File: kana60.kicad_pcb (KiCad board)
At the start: 2 copper layers, 285.4 x 115.5 mm, 148 parts, among them SW1 SW_PUSH, SW10 SW_PUSH, SW11 SW_PUSH, SW12 SW_PUSH, SW13 SW_PUSH, SW14 SW_PUSH, SW15 SW_PUSH, SW16 SW_PUSH, SW17 SW_PUSH, SW18 SW_PUSH, SW19 SW_PUSH, SW2 SW_PUSH, SW20 SW_PUSH, SW21 SW_PUSH, SW22 SW_PUSH, SW23 SW_PUSH, SW24 SW_PUSH, SW25 SW_PUSH, SW26 SW_PUSH, SW27 SW_PUSH, SW28 SW_PUSH, SW29 SW_PUSH, SW3 SW_PUSH, SW30 SW_PUSH, SW31 SW_PUSH, SW32 SW_PUSH, SW33 SW_PUSH, SW34 SW_PUSH, SW35 SW_PUSH, SW36 SW_PUSH, SW37 SW_PUSH, SW38 SW_PUSH, SW39 SW_PUSH, SW4 SW_PUSH, SW40 SW_PUSH, SW41 SW_PUSH, SW42 SW_PUSH, SW43 SW_PUSH, SW44 SW_PUSH, SW45 SW_PUSH, SW46 SW_PUSH, SW47 SW_PUSH, SW48 SW_PUSH, SW49 SW_PUSH, SW5 SW_PUSH, SW50 SW_PUSH, SW51 SW_PUSH, SW52 SW_PUSH, SW53 SW_PUSH, SW54 SW_PUSH, SW55 SW_PUSH, SW56 SW_PUSH, SW57 SW_PUSH, SW58 SW_PUSH, SW59 SW_PUSH, SW6 SW_PUSH, SW60 SW_PUSH, SW61 SW_PUSH, SW62 SW_PUSH, SW63 SW_PUSH, SW64 SW_PUSH, SW65 SW_PUSH, SW66 SW_PUSH, SW67 SW_PUSH, SW68 SW_PUSH, SW69 SW_PUSH, SW7 SW_PUSH, SW70 SW_PUSH, SW71 SW_Push, SW8 SW_PUSH, SW9 SW_PUSH, U1 ProMicro

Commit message: trial and error
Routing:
- net col0: track 247.0 -> 647.6 mm
- net col1: track 235.3 -> 553.2 mm
- net col2: track 252.0 -> 501.0 mm
- net col3: track 229.0 -> 455.6 mm
- net col4: track 213.3 -> 369.7 mm
- net col5: track 235.9 -> 382.3 mm
- net col6: track 151.2 -> 192.0 mm
- net row1-0: track 91.7 -> 90.2 mm
- net row1-1: track 71.1 -> 70.0 mm
- net reset: track 44.6 -> 43.5 mm
- net Net-(D57-Pad2): track 180.4 -> 179.4 mm
- net Net-(D58-Pad2): track 140.7 -> 140.2 mm

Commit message: update
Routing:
- net col0: track 647.6 -> 501.7 mm
- net col1: track 553.2 -> 452.5 mm
- net col5: track 382.3 -> 291.1 mm, vias 0 -> 2
- net col3: track 455.6 -> 378.8 mm, vias 0 -> 2
- net col2: track 501.0 -> 444.4 mm
- net col4: track 369.7 -> 313.1 mm, vias 0 -> 2
- net col6: track 192.0 -> 228.8 mm
- net Net-(D57-Pad2): track 179.4 -> 144.0 mm
- net rs: track 168.7 -> 158.2 mm
- net Net-(D67-Pad2): track 292.9 -> 284.0 mm
- net Net-(D19-Pad2): track 134.6 -> 126.7 mm
- net Net-(D21-Pad2): track 100.0 -> 92.2 mm
- net Net-(D17-Pad2): track 168.4 -> 161.1 mm
- net Net-(D30-Pad2): track 98.7 -> 91.7 mm
- net Net-(D20-Pad2): track 135.5 -> 129.0 mm
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
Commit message: update
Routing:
- net Net-(D53-Pad2): track 182.9 -> 188.6 mm
- net Net-(D51-Pad2): track 143.7 -> 149.4 mm
- net Net-(D55-Pad2): track 229.3 -> 234.3 mm
- net Net-(D27-Pad2): track 84.5 -> 87.5 mm
- net Net-(D41-Pad2): track 185.9 -> 188.3 mm
- net Net-(D22-Pad2): track 94.4 -> 96.8 mm
- net Net-(D40-Pad2): track 193.6 -> 195.9 mm
- net Net-(D39-Pad2): track 147.3 -> 149.6 mm
- net Net-(D49-Pad2): track 108.6 -> 110.7 mm
- net Net-(D47-Pad2): track 97.3 -> 99.3 mm
- net col2: track 444.4 -> 446.3 mm
- net Net-(D43-Pad2): track 163.7 -> 165.6 mm
- net Net-(D24-Pad2): track 71.2 -> 72.8 mm
- net Net-(D42-Pad2): track 237.1 -> 238.3 mm
- net Net-(D20-Pad2): track 129.0 -> 130.2 mm
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
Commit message: connection complete
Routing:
- net row4-1: track 211.6 -> 206.1 mm
- net col2: track 446.3 -> 450.7 mm
- net col4: track 313.2 -> 316.6 mm
- net row2-1: track 192.8 -> 189.5 mm
- net row3-0: track 171.5 -> 169.0 mm
- net col3: track 378.8 -> 381.0 mm
- net row0-0: track 129.8 -> 128.0 mm
- net col0: track 501.7 -> 503.3 mm
- net col1: track 452.6 -> 454.1 mm
- net row2-0: track 150.0 -> 148.5 mm
- net col5: track 291.1 -> 292.5 mm
- net row1-0: track 90.5 -> 91.9 mm
- net row1-1: track 70.2 -> 71.4 mm
- net reset: track 44.1 -> 43.6 mm

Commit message: rotate reset switch
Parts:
- moved SW71 2.70 mm to (260.9, 21.8), turned to 180 degrees
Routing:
- net col4: track 316.6 -> 313.6 mm
- net reset: track 43.6 -> 46.1 mm
- net col3: track 381.0 -> 378.9 mm
- net col2: track 450.7 -> 448.8 mm
- net col1: track 454.1 -> 452.5 mm
- net col0: track 503.3 -> 502.0 mm
- net row1-1: track 71.4 -> 70.7 mm
- net row1-0: track 91.9 -> 91.2 mm
- net row3-1: track 228.8 -> 228.3 mm
- net row4-0: track 245.9 -> 245.3 mm

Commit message: update
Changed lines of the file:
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@@
     (thickness 1.6)
     (drawings 655)
-    (tracks 1100)
+    (tracks 1095)
     (zones 0)
     (modules 148)
@@
   (segment (start 105.653978 38.55771) (end 163.30722 38.55771) (width 0.25) (layer B.Cu) (net 9))
   (segment (start 25.71 25.7677) (end 42.49015 25.7677) (width 0.25) (layer B.Cu) (net 10))
-  (segment (start 42.49015 25.7677) (end 44.39515 23.8627) (width 0.25) (layer F.Cu) (net 10))
-  (segment (start 250.862288 26.416) (end 255.915688 26.416) (width 0.25) (layer F.Cu) (net 10))
+  (segment (start 262.900688 26.416) (end 265.453988 23.8627) (width 0.25) (layer F.Cu) (net 10))
   (segment (start 248.308988 23.8627) (end 250.862288 26.416) (width 0.25) (layer F.Cu) (net 10))
-  (segment (start 255.915688 26.416) (end 258.468988 23.8627) (width 0.25) (layer F.Cu) (net 10))
   (segment (start 265.453988 23.8627) (end 267.358988 21.9577) (width 0.25) (layer F.Cu) (net 10))
-  (segment (start 258.468988 23.8627) (end 265.453988 23.8627) (width 0.25) (layer F.Cu) (net 10))
+  (segment (start 42.49015 25.7677) (end 44.39515 23.8627) (width 0.25) (layer F.Cu) (net 10))
   (segment (start 44.39515 23.8627) (end 248.308988 23.8627) (width 0.25) (layer F.Cu) (net 10))
+  (segment (start 250.862288 26.416) (end 262.900688 26.416) (width 0.25) (layer F.Cu) (net 10))
   (segment (start 186.79944 39.00656) (end 186.79944 33.3877) (width 0.25) (layer B.Cu) (net 11))
   (segment (start 186.182 39.624) (end 186.79944 39.00656) (width 0.25) (layer B.Cu) (net 11))
@@
   (segment (start 170.01929 33.3877) (end 170.01929 41.593002) (width 0.25) (layer F.Cu) (net 17))
   (segment (start 45.84618 25.7677) (end 62.62633 25.7677) (width 0.25) (layer B.Cu) (net 18))
-  (segment (start 257.058688 27.178) (end 259.103988 25.1327) (width 0.25) (layer F.Cu) (net 18))
-  (segment (start 269.263988 25.1327) (end 269.898988 24.4977) (width 0.25) (layer F.Cu) (net 18))
-  (segment (start 64.03663 27.178) (end 257.058688 27.178) (width 0.25) (layer F.Cu) (net 18))
   (segment (start 269.898988 24.4977) (end 269.898988 21.9577) (width 0.25) (layer F.Cu) (net 18))
-  (segment (start 259.103988 25.1327) (end 269.263988 25.1327) (width 0.25) (layer F.Cu) (net 18))
+  (segment (start 267.218688 27.178) (end 269.898988 24.4977) (width 0.25) (layer F.Cu) (net 18))
+  (segment (start 64.03663 27.178) (end 267.218688 27.178) (width 0.25) (layer F.Cu) (net 18))
   (segment (start 62.62633 25.7677) (end 64.03663 27.178) (width 0.25) (layer F.Cu) (net 18))
   (segment (start 193.5115 45.950188) (end 193.468988 45.9927) (width 0.25) (layer F.Cu) (net 19))
@@
   (segment (start 47.752 45.230712) (end 47.752 54.755712) (width 0.25) (layer F.Cu) (net 75))
   (segment (start 46.993988 44.4727) (end 47.752 45.230712) (width 0.25) (layer F.Cu) (net 75))
+  (segment (start 47.498 28.448) (end 47.498 43.968688) (width 0.25) (layer F.Cu) (net 75))
   (segment (start 47.498 43.968688) (end 46.993988 44.4727) (width 0.25) (layer F.Cu) (net 75))
-  (segment (start 47.498 28.956) (end 47.498 43.968688) (width 0.25) (layer F.Cu) (net 75))
   (segment (start 282.598988 21.9577) (end 282.598988 27.535012) (width 0.25) (layer F.Cu) (net 75))
-  (segment (start 282.194 27.94) (end 48.514 27.94) (width 0.25) (layer F.Cu) (net 75))
-  (segment (start 48.514 27.94) (end 47.498 28.956) (width 0.25) (layer F.Cu) (net 75))
+  (segment (start 48.006 27.94) (end 47.498 28.448) (width 0.25) (layer F.Cu) (net 75))
+  (segment (start 282.194 27.94) (end 48.006 27.94) (width 0.25) (layer F.Cu) (net 75))
   (segment (start 282.598988 27.535012) (end 282.194 27.94) (width 0.25) (layer F.Cu) (net 75))
   (segment (start 80.021488 120.6727) (end 77.950238 120.6727) (width 0.25) (layer F.Cu) (net 76))
@@
   (segment (start 100.076 92.792212) (end 100.076 83.267212) (width 0.25) (layer F.Cu) (net 76))
   (segment (start 108.906488 101.6227) (end 100.076 92.792212) (width 0.25) (layer F.Cu) (net 76))
-  (segment (start 86.36 29.083) (end 86.741 28.702) (width 0.25) (layer F.Cu) (net 76))
-  (segment (start 84.455 29.591) (end 84.963 29.083) (width 0.25) (layer F.Cu) (net 76))
-  (segment (start 84.455 43.833712) (end 84.455 29.591) (width 0.25) (layer F.Cu) (net 76))
   (segment (start 285.138988 28.297012) (end 285.138988 21.9577) (width 0.25) (layer F.Cu) (net 76))
   (segment (start 284.734 28.702) (end 285.138988 28.297012) (width 0.25) (layer F.Cu) (net 76))
-  (segment (start 86.741 28.702) (end 284.734 28.702) (width 0.25) (layer F.Cu) (net 76))
-  (segment (start 84.963 29.083) (end 86.36 29.083) (width 0.25) (layer F.Cu) (net 76))
+  (segment (start 84.455 29.21) (end 84.963 28.702) (width 0.25) (layer F.Cu) (net 76))
   (segment (start 85.093988 44.4727) (end 84.455 43.833712) (width 0.25) (layer F.Cu) (net 76))
+  (segment (start 84.455 43.833712) (end 84.455 29.21) (width 0.25) (layer F.Cu) (net 76))
+  (segment (start 84.963 28.702) (end 284.734 28.702) (width 0.25) (layer F.Cu) (net 76))
   (segment (start 114.323988 78.4652) (end 118.431488 82.5727) (width 0.25) (layer F.Cu) (net 77))
   (segment (start 114.323988 64.1777) (end 114.323988 78.4652) (width 0.25) (layer F.Cu) (net 77))
@@
   (segment (start 119.126 98.806) (end 120.142 99.822) (width 0.25) (layer F.Cu) (net 77))
   (segment (start 118.431488 82.5727) (end 119.126 83.267212) (width 0.25) (layer F.Cu) (net 77))
-  (segment (start 125.476 39.624) (end 123.193988 41.906012) (width 0.25) (layer F.Cu) (net 77))
   (segment (start 123.193988 41.906012) (end 123.193988 44.4727) (width 0.25) (layer F.Cu) (net 77))
+  (segment (start 125.476 39.624) (end 123.193988 41.906012) (width 0.25) (layer F.Cu) (net 77))
   (segment (start 128.778 39.624) (end 125.476 39.624) (width 0.25) (layer F.Cu) (net 77))
+  (segment (start 131.445 30.099) (end 131.445 36.957) (width 0.25) (layer F.Cu) (net 77))
+  (segment (start 132.08 29.464) (end 131.445 30.099) (width 0.25) (layer F.Cu) (net 77))
   (segment (start 292.758988 29.059012) (end 292.354 29.464) (width 0.25) (layer F.Cu) (net 77))
-  (segment (start 132.334 29.464) (end 131.445 30.353) (width 0.25) (layer F.Cu) (net 77))
-  (segment (start 292.354 29.464) (end 132.334 29.464) (width 0.25) (layer F.Cu) (net 77))
   (segment (start 131.445 36.957) (end 128.778 39.624) (width 0.25) (layer F.Cu) (net 77))
-  (segment (start 131.445 30.353) (end 131.445 36.957) (width 0.25) (layer F.Cu) (net 77))
+  (segment (start 292.354 29.464) (end 132.08 29.464) (width 0.25) (layer F.Cu) (net 77))
   (segment (start 292.758988 21.9577) (end 292.758988 29.059012) (width 0.25) (layer F.Cu) (net 77))
   (segment (start 290.218988 25.042988) (end 290.218988 37.1977) (width 0.25) (layer B.Cu) (net 78))
@@
   (via (at 280.058988 30.988) (size 0.8) (drill 0.4) (layers F.Cu B.Cu) (net 80))
   (segment (start 279.296988 30.226) (end 280.058988 30.988) (width 0.25) (layer F.Cu) (net 80))
-  (segment (start 162.306 30.226) (end 279.296988 30.226) (width 0.25) (layer F.Cu) (net 80))
-  (segment (start 161.293988 31.238012) (end 162.306 30.226) (width 0.25) (layer F.Cu) (net 80))
-  (segment (start 161.293988 44.4727) (end 161.293988 31.238012) (width 0.25) (layer F.Cu) (net 80))
+  (segment (start 162.052 30.226) (end 279.296988 30.226) (width 0.25) (layer F.Cu) (net 80))
+  (segment (start 161.293988 30.984012) (end 162.052 30.226) (width 0.25) (layer F.Cu) (net 80))
+  (segment (start 161.293988 44.4727) (end 161.293988 30.984012) (width 0.25) (layer F.Cu) (net 80))
   (segment (start 257.198988 128.1297) (end 257.198988 121.3277) (width 0.25) (layer B.Cu) (net 81))
   (segment (start 238.021988 128.0027) (end 238.529988 128.5107) (width 0.25) (layer B.Cu) (net 81))

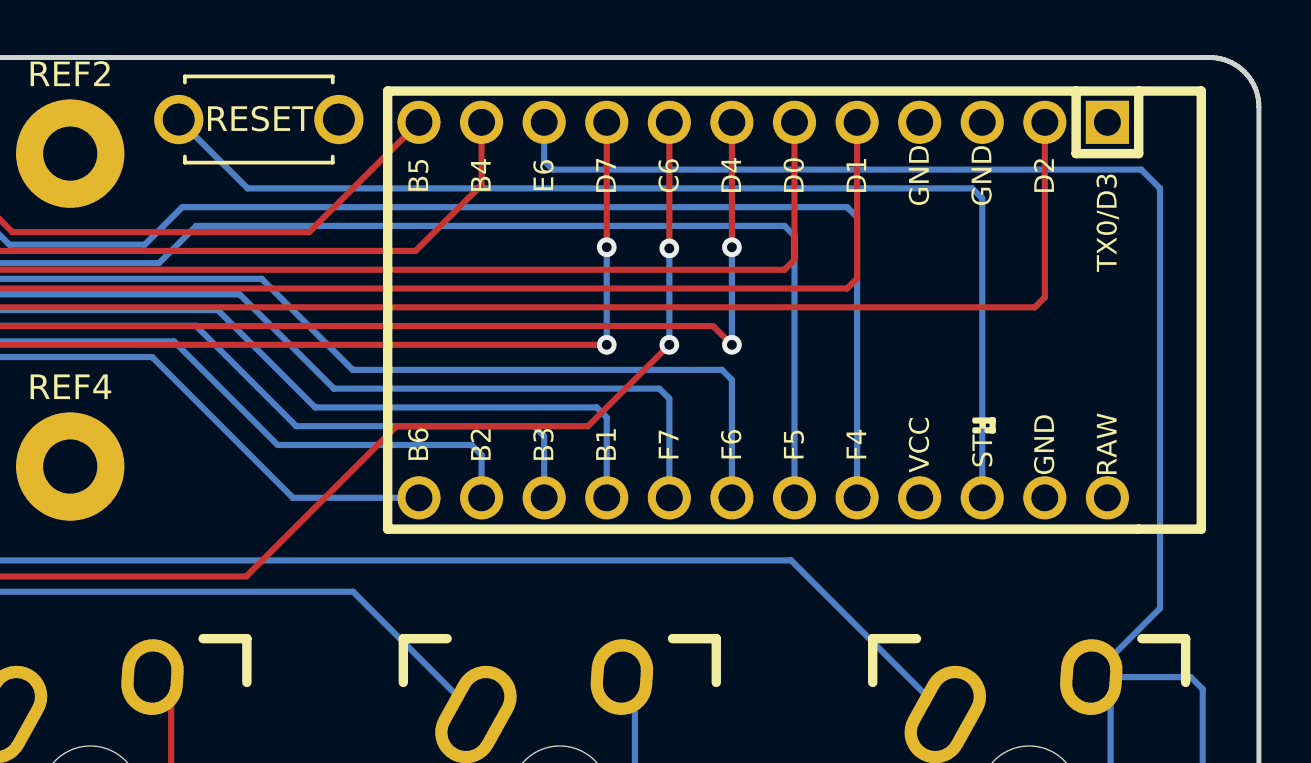
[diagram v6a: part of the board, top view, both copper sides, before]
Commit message: add text
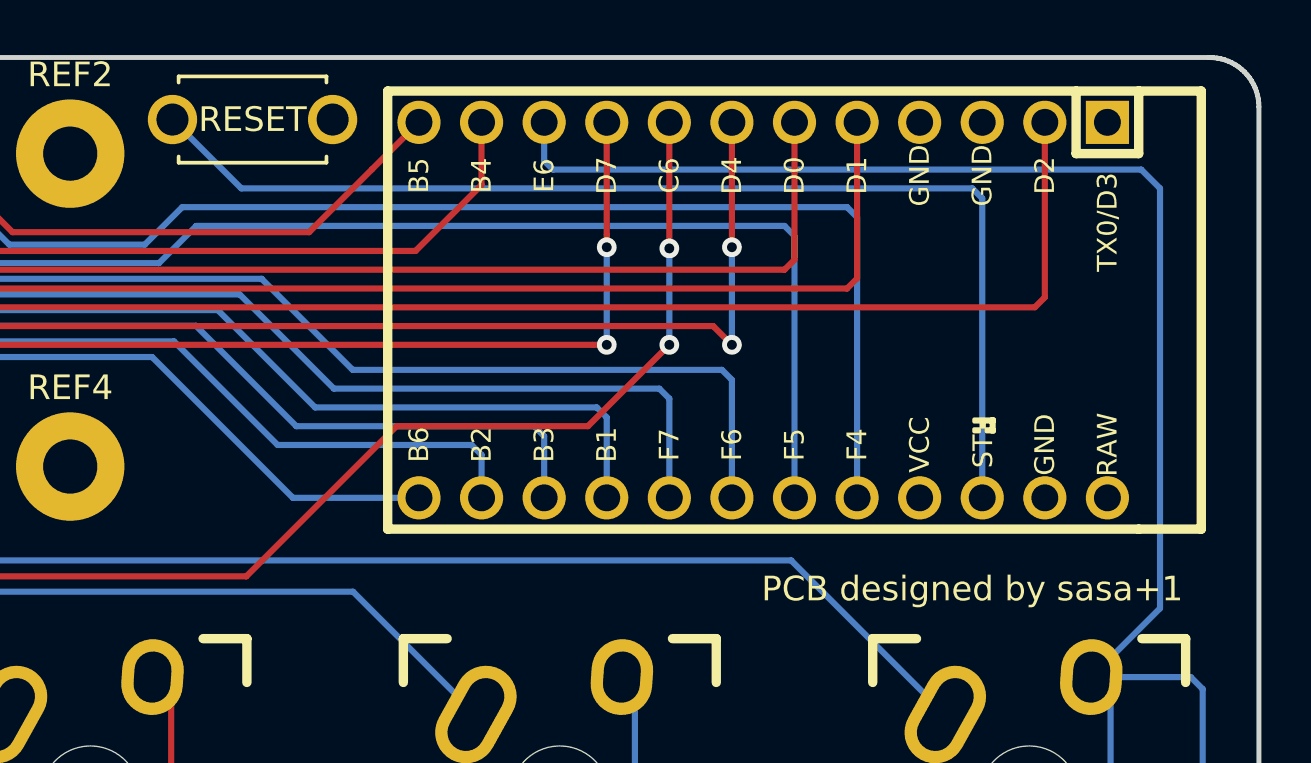
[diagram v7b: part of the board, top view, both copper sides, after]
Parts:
- moved SW71 0.25 mm to (260.6, 21.8)
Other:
- board text added: "PCB designed by sasa+1"
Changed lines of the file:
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@@
   (general
     (thickness 1.6)
-    (drawings 655)
+    (drawings 656)
     (tracks 1095)
     (zones 0)
@@
       (padsonsilk false)
       (subtractmaskfromsilk false)
-      (outputformat 1)
+      (outputformat 4)
       (mirror false)
-      (drillshape 1)
+      (drillshape 0)
       (scaleselection 1)
       (outputdirectory ""))
@@
   )
   (module kbd:ResetSW (layer F.Cu)
-    (at 260.858 21.844 180)
+    (at 260.604 21.844 180)
     (fp_text reference SW71 (at 0 2.55) (layer F.SilkS) hide
       (effects (font (size 1 1) (thickness 0.15)))
@@
       (net 20 row4-1))
   )
+  (gr_text "PCB designed by sasa+1" (at 289.814 40.894) (layer F.SilkS)
+    (effects (font (size 1 1) (thickness 0.15)))
+  )
   (gr_line (start 18.07122 19.3255) (end 299.4476 19.3269) (layer Edge.Cuts) (width 0.2))
   (gr_line (start 17.9155 19.3322) (end 18.07122 19.3255) (layer Edge.Cuts) (width 0.2))
@@
   (segment (start 292.758988 21.9577) (end 292.758988 29.059012) (width 0.25) (layer F.Cu) (net 77))
   (segment (start 290.218988 25.042988) (end 290.218988 37.1977) (width 0.25) (layer B.Cu) (net 78))
-  (segment (start 260.402 24.638) (end 289.814 24.638) (width 0.25) (layer B.Cu) (net 78))
-  (segment (start 257.608 21.844) (end 260.402 24.638) (width 0.25) (layer B.Cu) (net 78))
   (segment (start 289.814 24.638) (end 290.218988 25.042988) (width 0.25) (layer B.Cu) (net 78))
+  (segment (start 260.148 24.638) (end 289.814 24.638) (width 0.25) (layer B.Cu) (net 78))
+  (segment (start 257.354 21.844) (end 260.148 24.638) (width 0.25) (layer B.Cu) (net 78))
   (segment (start 192.809988 128.0027) (end 192.809988 121.23245) (width 0.25) (layer B.Cu) (net 80))
   (segment (start 192.809988 121.23245) (end 192.250238 120.6727) (width 0.25) (layer B.Cu) (net 80))
